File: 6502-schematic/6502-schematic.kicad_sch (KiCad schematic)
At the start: 16 parts, among them U1 W65C02S, U2 W65C22, U3 AT28C256, U4 AS6C62256, U5 SN74HCT00N, Y1 ecs-2100x

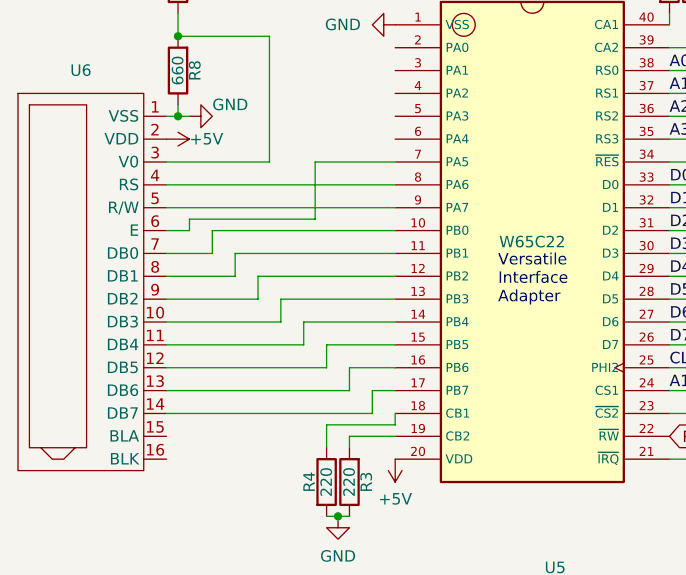
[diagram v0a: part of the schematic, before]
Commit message: Changed LCD interface and code to 4-bit mode
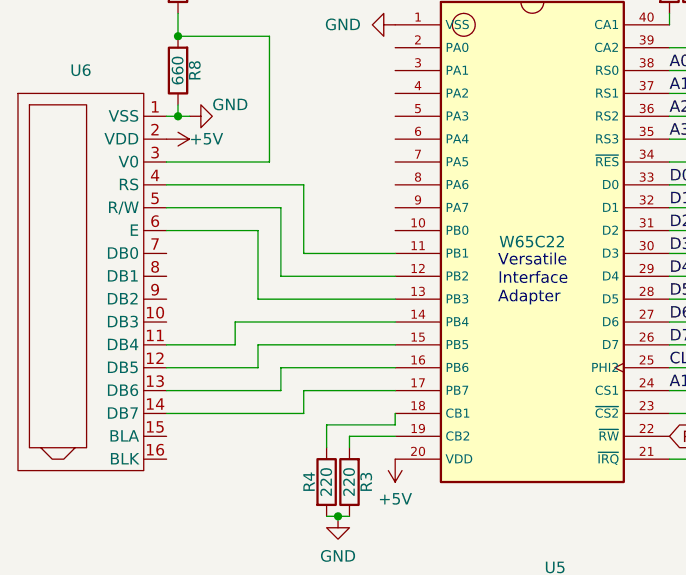
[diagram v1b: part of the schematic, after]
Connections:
- net at U6.10 (DB3): no longer U2.13 (PB3)
- net at U6.4 (RS): now also U2.11 (PB1); no longer U2.8 (PA6)
- net at U6.5 (R/W): now also U2.12 (PB2); no longer U2.9 (PA7)
- net at U6.6 (E): now also U2.13 (PB3); no longer U2.7 (PA5)
- net at U6.7 (DB0): no longer U2.10 (PB0)
- net at U6.8 (DB1): no longer U2.11 (PB1)
- net at U6.9 (DB2): no longer U2.12 (PB2)

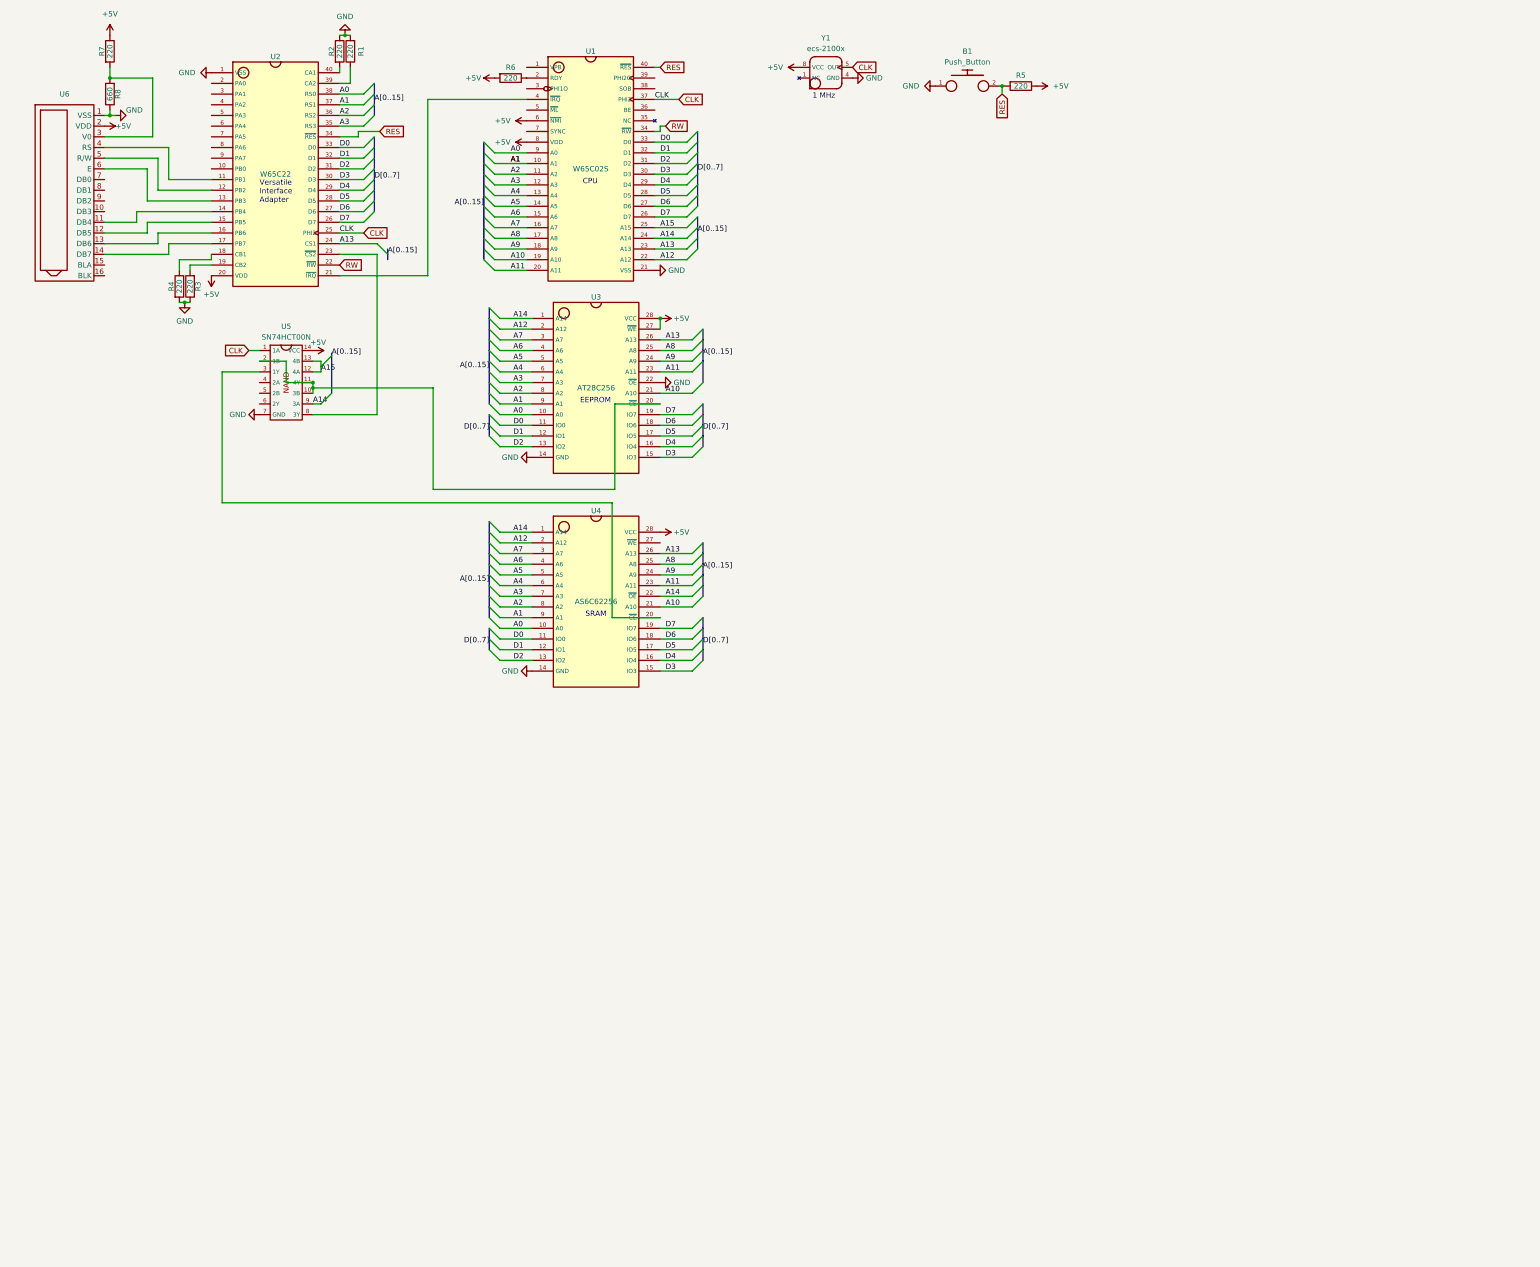
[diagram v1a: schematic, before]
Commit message: A lot of changes...
Re drew the schematic, now contains an extra EEPROM which handles address  glue logic.

arduino debugger now decodes instructions on the databus

Some new scripts which generate the address map for the new EEPROM gluelogic
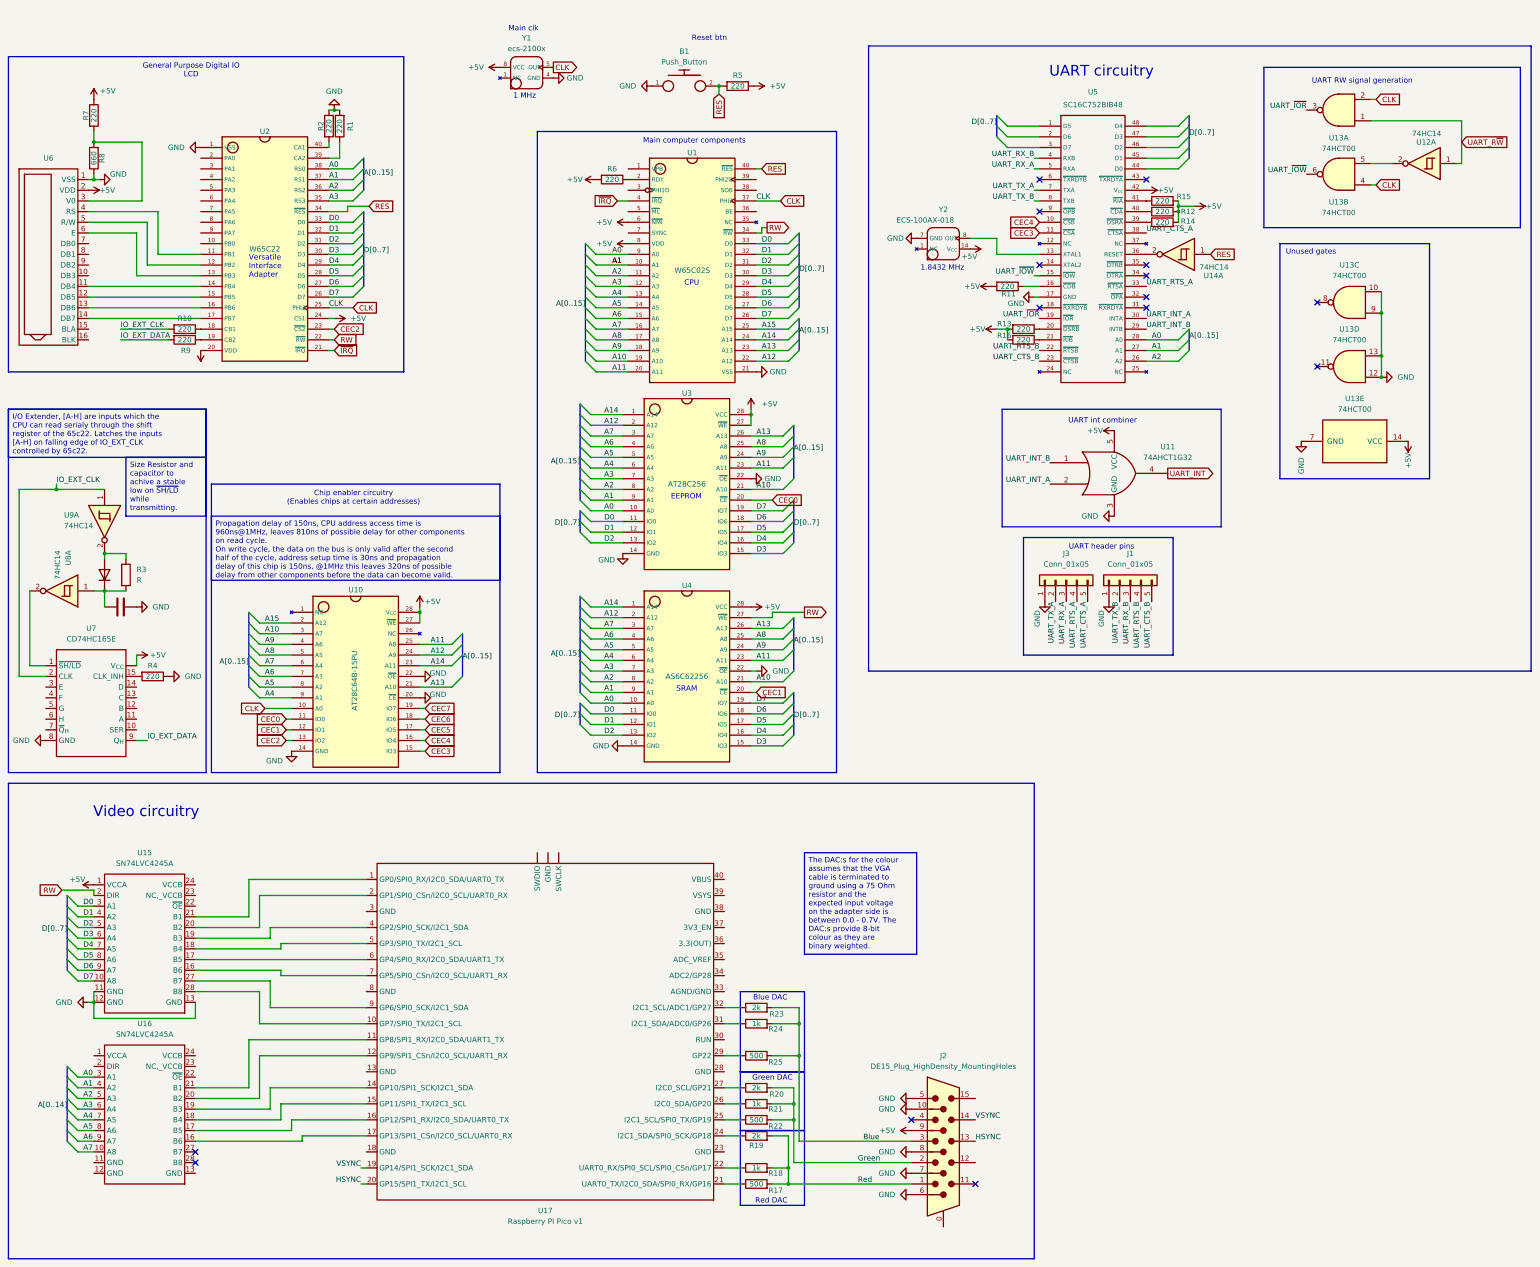
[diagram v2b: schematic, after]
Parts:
- removed U5: SN74HCT00N, symbol 6502-and-friends:SN74HCT00N
- added C1: C, symbol Device:C
- added D1: D, symbol Device:D
- added J1, J3: Conn_01x05, Connector_PinHeader_2.54mm:PinHeader_1x05_P2.54mm_Vertical, symbol Connector_Generic:Conn_01x05
- added J2: DE15_Plug_HighDensity_MountingHoles, Connector_Dsub:DSUB-15-HD_Female_Horizontal_P2.29x1.98mm_EdgePinOffset3.03mm_Housed_MountingHolesOffset4.94mm, symbol Connector:DE15_Plug_HighDensity_MountingHoles
- added R10, R11, R12, R13, R14, R15, R16, R9: 220, symbol Device:R
- added R17, R22, R25: 500, symbol Device:R
- added R18, R21, R24: 1k, symbol Device:R
- added R19, R20, R23: 2k, symbol Device:R
- added U10: AT28C64B-15PU, Package_DIP:DIP-28_W15.24mm_LongPads, symbol 6502-and-friends:AT28C64B-15PU
- added U11: 74AHCT1G32, symbol 74xGxx:74AHCT1G32
- added U12, U14, U8, U9: 74HC14, symbol 74xx:74HC14
- added U13: 74HCT00, Package_DIP:DIP-14_W7.62mm_LongPads, symbol 74xx:74HCT00
- added U15, U16: SN74LVC4245A, Package_SO:SOIC-24W_7.5x15.4mm_P1.27mm, symbol 6502-and-friends:SN74LVC4245A
- added U17: Raspberry PI Pico v1, symbol 6502-and-friends:raspberry_pi_pico_v1
- added U5: SC16C752BIB48, Package_QFP:LQFP-48_7x7mm_P0.5mm, symbol 6502-and-friends:SC16C752BIB48
- added U7: CD74HC165E, Package_DIP:DIP-16_W7.62mm_LongPads, symbol 6502-and-friends:CD74HC165
- added Y2: ECS-100AX-018, symbol 6502-and-friends:ECS-100AX-018
- R3: value 220 -> R
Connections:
- net +5V: now also U2.24 (CS1), J2.9, R11.2, R12.2, R13.2, R14.2, R15.2, R16.2, U10.27 (~{WE}), U10.28 (V_{CC}), U11.5 (VCC), U13.14 (VCC), U15.1 (VCCA), U5.42 (V_{cc}), U7. (V_{CC}), Y2.14 (V_{CC})
- net A0: now also U16.3 (A1), U5.28 (A0)
- net A1: now also U16.4 (A2), U5.27 (A1)
- net A10: now also U10.3 (A7)
- net A11: now also U10.25 (A8)
- net A12: now also U10.24 (A9)
- net A13: now also U10.21 (A10); no longer U2.24 (CS1)
- net A14: now also U10.23 (A11); no longer U4.22 (~{OE})
- net A15: now also U10.2 (A12)
- net A2: now also U16.5 (A3), U5.26 (A2)
- net A3: now also U16.6 (A4)
- net A4: now also U10.9 (A1), U16.7 (A5)
- net A5: now also U10.8 (A2), U16.8 (A6)
- net A6: now also U10.7 (A3), U16.9 (A7)
- net A7: now also U10.6 (A4), U16.10 (A8)
- net A8: now also U10.5 (A5)
- net A9: now also U10.4 (A6)
- net CLK: now also U10.10 (A0), U13.2, U13.4
- net D0: now also U15.3 (A1)
- net D1: now also U15.4 (A2)
- net D2: now also U15.5 (A3)
- net D3: now also U15.6 (A4)
- net D4: now also U15.7 (A5)
- net D5: now also U15.8 (A6)
- net D6: now also U15.9 (A7)
- net D7: now also U15.10 (A8)
- net GND: now also R4.1, U4.22 (~{OE}), C1.2, J1.1 (Pin_1), J2.10, J2.5, J2.6, J2.7, J2.8, J3.1 (Pin_1), U10.14 (GND), U10.20 (~{CE}), U10.22 (~{OE}), U11.3 (GND), U13.10, U13.12, U13.13, U13.7 (GND), U13.9, U15.11 (GND), U15.12 (GND), U15.13 (GND), U5.17 (GND), U7.8 (GND), Y2.7 (GND); no longer R3.1, R4.2
- net RES: now also U14.1
- net RW: now also U4.27 (~{WE}), U15.2 (DIR)
- net ~{IRQ}: now reaches U1.4 (~{IRQ}), U2.21 (~{IRQ})
- net at U2.18 (CB1): now also R10.1; no longer R4.1
- net at U2.19 (CB2): now also R9.1; no longer R3.2
- net CEC1: now reaches U4.20 (~{CE})
- net CEC1: now also U10.12 (IO1)
- net CEC0: now reaches U3.20 (~{CE})
- net CEC0: now also U10.11 (IO0)
- net CEC2: now reaches U2.23 (~{CS2})
- net CEC2: now also U10.13 (IO2)
- new net: D1.2 (A), R3.1, U9.2
- new net: U16.16 (B6), U17.17 (GP13/SPI1_CSn/I2C0_SCL/UART0_RX)
- new net: U16.17 (B5), U17.16 (GP12/SPI1_RX/I2C0_SDA/UART0_TX)
- new net: U16.18 (B4), U17.15 (GP11/SPI1_TX/I2C1_SCL)
- new net: U16.19 (B3), U17.14 (GP10/SPI1_SCK/I2C1_SDA)
- new net: U16.20 (B2), U17.12 (GP9/SPI1_CSn/I2C0_SCL/UART1_RX)
- new net: U16.21 (B1), U17.11 (GP8/SPI1_RX/I2C0_SDA/UART1_TX)
- new net: U14.2, U5.36 (RESET)
- new net: U12.2, U13.5
- new net: R17.1, U17.21 (UART0_TX/I2C0_SDA/SPI0_RX/GP16)
- new net: R4.2, U7.15 (CLK_INH)
- new net: R16.1, U5.21 (~{RIB})
- new net: R11.1, U5.16 (~{CDB})
- new net: R20.1, U17.27 (I2C0_SCL/GP21)
- new net: U15.16 (B6), U17.7 (GP5/SPI0_CSn/I2C0_SCL/UART1_RX)
- new net: U15.17 (B5), U17.6 (GP4/SPI0_RX/I2C0_SDA/UART1_TX)
- new net: U15.18 (B4), U17.5 (GP3/SPI0_TX/I2C1_SCL)
- new net: U15.19 (B3), U17.4 (GP2/SPI0_SCK/I2C1_SDA)
- new net: U15.20 (B2), U17.2 (GP1/SPI0_CSn/I2C0_SCL/UART0_RX)
- new net: U15.21 (B1), U17.1 (GP0/SPI0_RX/I2C0_SDA/UART0_TX)
- new net: U15.27 (B7), U17.9 (GP6/SPI0_SCK/I2C1_SDA)
- new net: U15.28 (B8), U17.10 (GP7/SPI0_TX/I2C1_SCL)
- new net: R23.1, U17.32 (I2C1_SCL/ADC1/GP27)
- new net: R21.1, U17.26 (I2C0_SDA/GP20)
- new net: R22.1, U17.25 (I2C1_SCL/SPI0_TX/GP19)
- new net: R13.1, U5.20 (~{DSRB})
- new net: C1.1, D1.1 (K), R3.2, U8.1
- new net: U5.13 (XTAL1), Y2.8 (OUT)
- new net: U7.1 (~{SH/LD}), U8.2
- new net: R25.1, U17.29 (GP22)
- new net: R14.1, U5.39 (~{DSRA})
- new net: R12.1, U5.40 (~{CDA})
- new net: R15.1, U5.41 (~{RIA})
- new net: R19.1, U17.24 (I2C1_SDA/SPI0_SCK/GP18)
- new net: R18.1, U17.22 (UART0_RX/SPI0_SCL/SPI0_CSn/GP17)
- new net: R24.1, U17.31 (I2C1_SDA/ADC0/GP26)
- new net Blue: J2.3, R23.2, R24.2, R25.2
- new net CEC3: U10.15 (IO3), U5.11 (~{CSA})
- new net CEC4: U10.16 (IO4), U5.10 (~{CSB})
- new net CEC5: U10.17 (IO5)
- new net CEC6: U10.18 (IO6)
- new net CEC7: U10.19 (IO7)
- new net Green: J2.2, R20.2, R21.2, R22.2
- new net HSYNC: J2.13, U17.20 (GP15/SPI1_TX/I2C1_SCL)
- new net IO_EXT_CLK: R10.2, U7.2 (CLK), U9.1
- new net IO_EXT_DATA: R9.2, U7.9 (Q_{H})
- new net Red: J2.1, R17.2, R18.2, R19.2
- new net UART_CTS_A: J3.5 (Pin_5), U5.38 (~{CTSA})
- new net UART_CTS_B: J1.5 (Pin_5), U5.23 (~{CTSB})
- new net UART_INT: U11.4
- new net UART_INT_A: U11.2, U5.30 (INTA)
- new net UART_INT_B: U11.1, U5.29 (INTB)
- new net UART_RTS_A: J3.4 (Pin_4), U5.33 (~{RTSA})
- new net UART_RTS_B: J1.4 (Pin_4), U5.22 (~{RTSB})
- new net UART_RX_A: J3.3 (Pin_3), U5.5 (RXA)
- new net UART_RX_B: J1.3 (Pin_3), U5.4 (RXB)
- new net UART_R~{W}: U12.1, U13.1
- new net UART_TX_A: J3.2 (Pin_2), U5.7 (TXA)
- new net UART_TX_B: J1.2 (Pin_2), U5.8 (TXB)
- new net UART_~{IOR}: U13.3, U5.19 (~{IOR})
- new net UART_~{IOW}: U13.6, U5.15 (~{IOW})
- new net VSYNC: J2.14, U17.19 (GP14/SPI1_SCK/I2C1_SDA)
- no-connect marks 0 -> 15
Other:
- note added: "1.8432 MHz"
- note added: "Blue DAC"
- note added: "Chip enabler circuitry (Enables chips at certain addresses)"
- note added: "General Purpose Digital IO LCD"
- note added: "Green DAC"
- note added: "Main clk"
- note added: "Main computer components"
- note added: "Red DAC"
- note added: "Reset btn"
- note added: "UART RW signal generation"
- note added: "UART circuitry"
- note added: "UART header pins"
- note added: "UART int combiner"
- note added: "Unused gates"
- note added: "Video circuitry"
- moved on the sheet: B1, R1, R2, R5, R6, R7, R8, U1, U2, U3, U4, U6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

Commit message: Finished schematic
Finished wiring up Raspberry pico up to the databus

Added debug connectors

set the footprint of all symbols

Started with layout
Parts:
- removed U12, U14, U8, U9: 74HC14, symbol 74xx:74HC14
- removed Y2: ECS-100AX-018, symbol 6502-and-friends:ECS-100AX-018
- added J4, J6, J9: Conn_01x08, Connector_PinHeader_2.54mm:PinHeader_1x08_P2.54mm_Vertical, symbol Connector_Generic:Conn_01x08
- added J5: Conn_01x16, Connector_PinHeader_2.54mm:PinHeader_1x16_P2.54mm_Vertical, symbol Connector_Generic:Conn_01x16
- added J7, J8: Conn_01x02, Connector_PinHeader_2.54mm:PinHeader_1x02_P2.54mm_Vertical, symbol Connector_Generic:Conn_01x02
- added R26, R27: 0, Resistor_SMD:R_0805_2012Metric_Pad1.20x1.40mm_HandSolder, symbol Device:R
- added R28: 1k, Resistor_THT:R_Axial_DIN0204_L3.6mm_D1.6mm_P2.54mm_Vertical, symbol Device:R
- added R29: 2k, Resistor_THT:R_Axial_DIN0204_L3.6mm_D1.6mm_P2.54mm_Vertical, symbol Device:R
- added U8: 74HC14, Package_DIP:CERDIP-14_W7.62mm_SideBrazed_LongPads, symbol 74xx:74HC14
- added Y2: ecs-2100x, 6502-and-friends:ECS-2100X, symbol 6502-and-friends:ECS-2100x
- B1: footprint (none) -> Button_Switch_THT:KSA_Tactile_SPST
- C1: footprint (none) -> Capacitor_THT:C_Disc_D9.0mm_W5.0mm_P10.00mm
- D1: footprint (none) -> Diode_THT:D_5W_P10.16mm_Horizontal
- J2: footprint Connector_Dsub:DSUB-15-HD_Female_Horizontal_P2.29x1.98mm_EdgePinOffset3.03mm_Housed_MountingHolesOffset4.94mm -> Connector_PinHeader_2.54mm:PinHeader_2x08_P2.54mm_Vertical
- R1, R10, R11, R12, R13, R14, R15, R16, R17, R18, R19, R2, R20, R21, R22, R23, R24, R25, R3, R4, R5, R6, R7, R8, R9: footprint (none) -> Resistor_THT:R_Axial_DIN0204_L3.6mm_D1.6mm_P2.54mm_Vertical
- U11: footprint (none) -> Package_TO_SOT_SMD:SOT-23-5_HandSoldering
- U17: footprint (none) -> 6502-and-friends:Raspberry_PI_Pico_Socket
- U6: footprint (none) -> Connector_PinHeader_2.54mm:PinHeader_1x16_P2.54mm_Vertical
- Y1: footprint (none) -> 6502-and-friends:ECS-2100X
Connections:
- net +5V: now also U16.1 (VCCA), U17.39 (VSYS), U7.16 (V_{CC}), J8.1 (Pin_1), U8.14 (VCC), Y2.4 (GND); no longer U7. (V_{CC})
- net A0: now also J5.1 (Pin_1)
- net A1: now also J5.2 (Pin_2)
- net A10: now also J5.11 (Pin_11)
- net A11: now also J5.12 (Pin_12)
- net A12: now also J5.13 (Pin_13)
- net A13: now also J5.14 (Pin_14)
- net A14: now also J5.15 (Pin_15)
- net A15: now also J5.16 (Pin_16)
- net A2: now also J5.3 (Pin_3)
- net A3: now also J5.4 (Pin_4)
- net A4: now also J5.5 (Pin_5)
- net A5: now also J5.6 (Pin_6)
- net A6: now also J5.7 (Pin_7)
- net A7: now also J5.8 (Pin_8)
- net A8: now also J5.9 (Pin_9)
- net A9: now also J5.10 (Pin_10)
- net CEC5: now also U15.22 (~{OE}), U16.22 (~{OE})
- net CLK: now also R26.2, R27.1; no longer Y1.5 (OUT)
- net D0: now also J6.1 (Pin_1)
- net D1: now also J6.2 (Pin_2)
- net D2: now also J6.3 (Pin_3)
- net D3: now also J6.4 (Pin_4)
- net D4: now also J6.5 (Pin_5)
- net D5: now also J6.6 (Pin_6)
- net D6: now also J6.7 (Pin_7)
- net D7: now also J6.8 (Pin_8)
- net GND: now also U16.11 (GND), U16.12 (GND), U16.13 (GND), U17.13 (GND), U17.18 (GND), U17.23 (GND), U17.28 (GND), U17.3 (GND), U17.8 (GND), J8.2 (Pin_2), R29.2, U8.11, U8.13, U8.7 (GND), Y2.8 (VCC)
- net IO_EXT_CLK: now also U8.3
- net RES: now also U8.5
- net RW: now also U16.2 (DIR), J7.1 (Pin_1), R28.2
- net UART_R~{W}: now also U8.9
- net at D1.2 (A), R3.1: now also U8.4
- net +3V3: now reaches U16.24 (VCCB)
- net +3V3: now also U15.24 (VCCB), U17.36 (3.3(OUT))
- net at U5.36 (RESET): now also U8.6
- net at U13.5: now also U8.8
- net at U17.9 (GP6/SPI0_SCK/I2C1_SDA): now also U15.15 (B7); no longer U15.27 (B7)
- net at U17.10 (GP7/SPI0_TX/I2C1_SCL): now also U15.14 (B8); no longer U15.28 (B8)
- net at C1.1, D1.1 (K), R3.2: now also U8.1
- net at U5.13 (XTAL1): now also Y2.5 (OUT)
- net at U7.1 (~{SH/LD}): now also U8.2
- net A: now reaches U7.11 (A)
- net A: now also J9.1 (Pin_1)
- net B: now reaches U7.12 (B)
- net B: now also J9.2 (Pin_2)
- net C: now reaches U7.13 (C)
- net C: now also J9.3 (Pin_3)
- net D: now reaches U7.14 (D)
- net D: now also J9.4 (Pin_4)
- net E: now reaches U7.3 (E)
- net E: now also J9.5 (Pin_5)
- net F: now reaches U7.4 (F)
- net F: now also J9.6 (Pin_6)
- net G: now reaches U7.5 (G)
- net G: now also J9.7 (Pin_7)
- net H: now reaches U7.6 (H)
- net H: now also J9.8 (Pin_8)
- net at U2.2 (PA0): now also J4.8 (Pin_8)
- net at U2.3 (PA1): now also J4.7 (Pin_7)
- net at U2.4 (PA2): now also J4.6 (Pin_6)
- net at U2.5 (PA3): now also J4.5 (Pin_5)
- net at U2.6 (PA4): now also J4.4 (Pin_4)
- net at U2.7 (PA5): now also J4.3 (Pin_3)
- net at U2.8 (PA6): now also J4.2 (Pin_2)
- net at U2.9 (PA7): now also J4.1 (Pin_1)
- net at U17.34 (ADC2/GP28): now also R28.1, R29.1
- new net: J7.2 (Pin_2), R27.2
- new net: R26.1, Y1.5 (OUT)
- no-connect marks 15 -> 34
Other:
- note added: "Debug connectors"
- moved on the sheet: R6, U1, U10, U13C, U13D, U13E, U3, U4
